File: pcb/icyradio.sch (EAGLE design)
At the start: 384 parts, among them CON301 FPC-40P, J701 TRSJACK, J702 TRSJACK, J703 TRSJACK, Q801 AO3400, Q802 AO3400, U1001 MIC23155, U1002 MIC23159, U1003 MIC2019, U1004 ADP150UJZ-1.8, U1005 ADP150UJZ-3.3, U1006 MIC94305, U1007 MIC94305, U101 EFM32GG11B420F2048GL112, U201 ATSAMS70Q21B-C, U301 ICE40HX8K-CT256, U302 SST26VF064B, U401 DSC1211DE3-C0017, U402 LTC2206, U403 RT820T2, U501 ADL5385, U502 AD9117, U503 ADL5601, U601 DSC1201DE3-50M00000, U602 ADF4351, U701 TSCS25A3X1NDGXZAX, U702 CP2615, U801 ER-TFT035-6, U901 DSC1201DE3-50M00000, U902 SI5351C, X101 32.768 kHz, X401 DNP, X901 DNP

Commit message: Production ready, ordered
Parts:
- removed R717, R718, R720, R721: 600 Ohms, Resistor:RESISTOR-0603
- removed R719, R722: 3.57 Ohms, Resistor:RESISTOR-0603
- added L701, L702, L703, L704, L705, L706: 600 Ohms, Inductor:INDUCTOR-0603
- R603: value 5.1K Ohm -> 5.1K Ohms
- U403: value RT820T2 -> R820T2; device Rafael Micro:RT820T2 -> Rafael Micro:R820T2
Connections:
- net CODEC_HP_L: now also L704.1; no longer R722.1
- net CODEC_HP_R: now also L703.1; no longer R719.1
- net CODEC_LINE_L: now also L706.1; no longer R721.1
- net CODEC_LINE_R: now also L702.1; no longer R718.1
- net CODEC_MIC_L: now also L705.1; no longer R720.1
- net CODEC_MIC_R: now also L701.1; no longer R717.1
- net N$38: now also L701.2; no longer R717.2
- net N$39: now also L705.2; no longer R720.2
- net N$42: now also L702.2; no longer R718.2
- net N$44: now also L706.2; no longer R721.2
- net N$50: now also L704.2; no longer R722.2
- net N$54: now also L703.2; no longer R719.2
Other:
- note added: "5th order Butterworth LPF fc = 10 MHz"
- note added: "FPGA_CLK1 = 49.152 MHz (for 48 kHz audio sample rate) FPGA_CLK1 = 45.1584 MHz (for 44.1 kHz audio sample rate) FPGA_CLK2 = TBD MHz (general purpose clock) FPGA_CLK3 = TBD MHz (general purpose clock) FPGA_CLK4 = TBD MHz (general purpose clock) SMC_MAIN_CLK = 50 MHz (SMC main clock) DSP_MAIN_CLK = 20 MHz (DSP main clock)"
- note added: "RXTUNER_REFCLK_SEL = 1 > 16 MHz (default) RXTUNER_REFCLK_SEL = 0 > 28.8 MHz"
- note removed: "FPGA_DDC_CLK = 49.152 MHz (for 48 kHz audio sample rate) FPGA_DDC_CLK = 45.1584 MHz (for 44.1 kHz audio sample rate) FPGA_GP_CLK1 = TBD MHz (general purpose clock) FPGA_GP_CLK2 = TBD MHz (general purpose clock) MCU_MAIN_CLK = TBD MHz (MCU main clock)"
- note removed: "TUNER_REFCLK_SEL = 1 > 16 MHz (default) TUNER_REFCLK_SEL = 0 > 28.8 MHz"
- moved on the sheet: SJ201

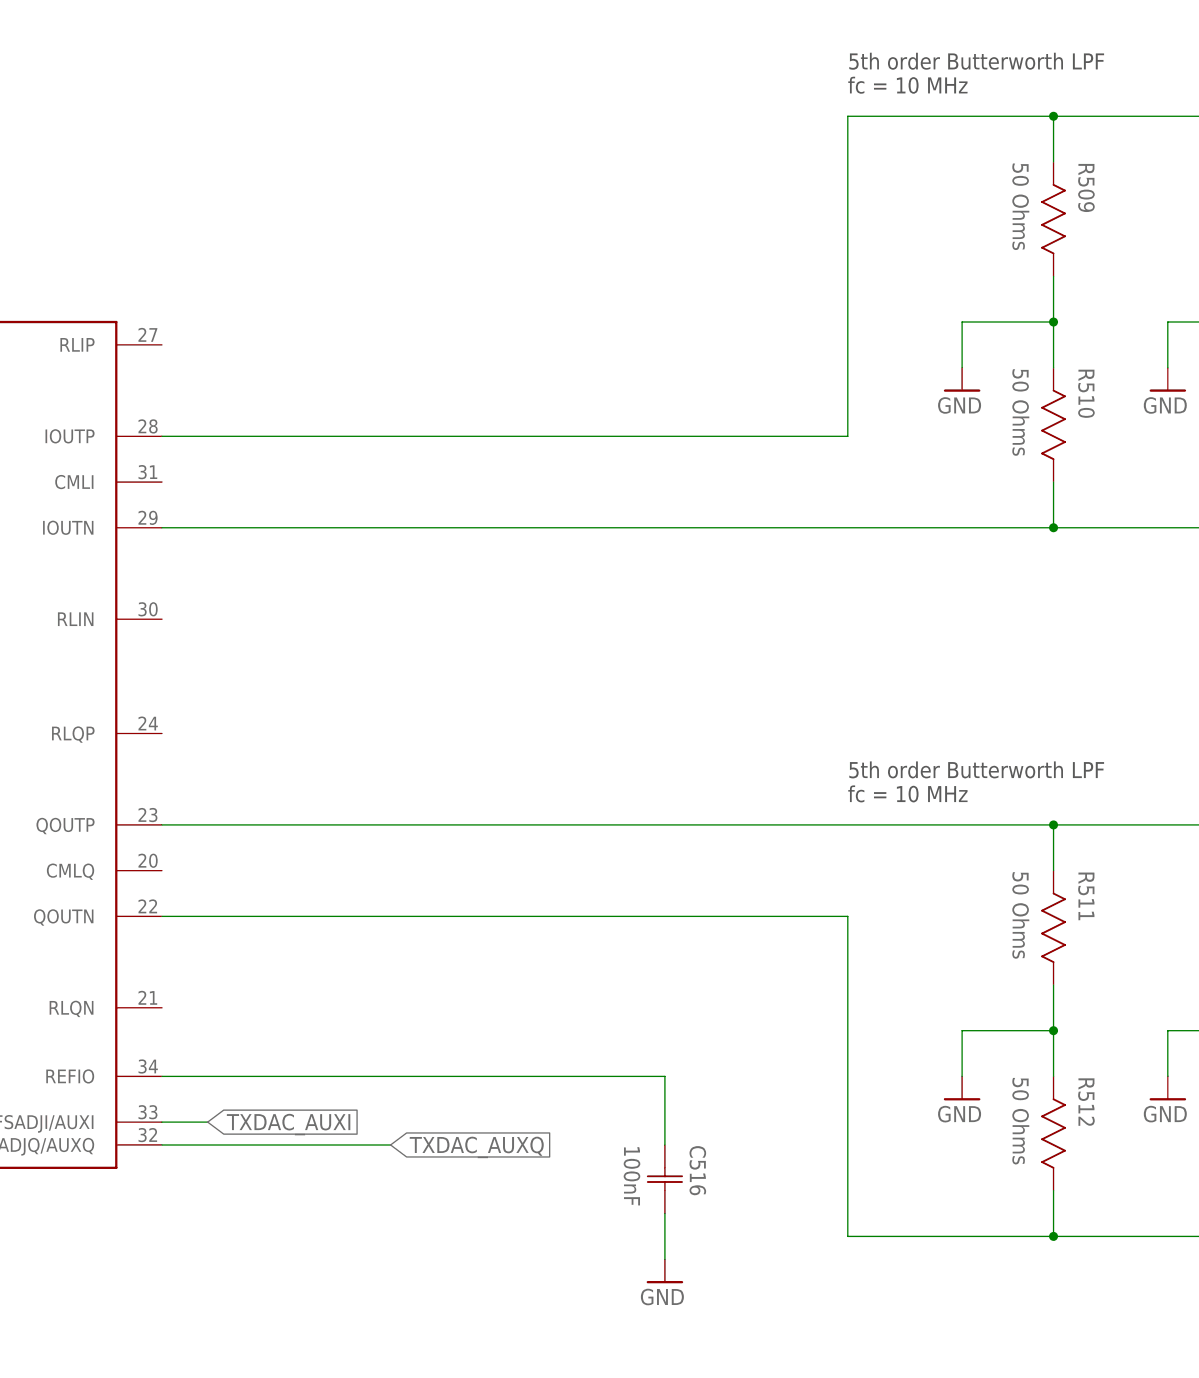
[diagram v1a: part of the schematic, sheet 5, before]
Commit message: Forgot to connect DAC common-mode, easy hardware fix tho
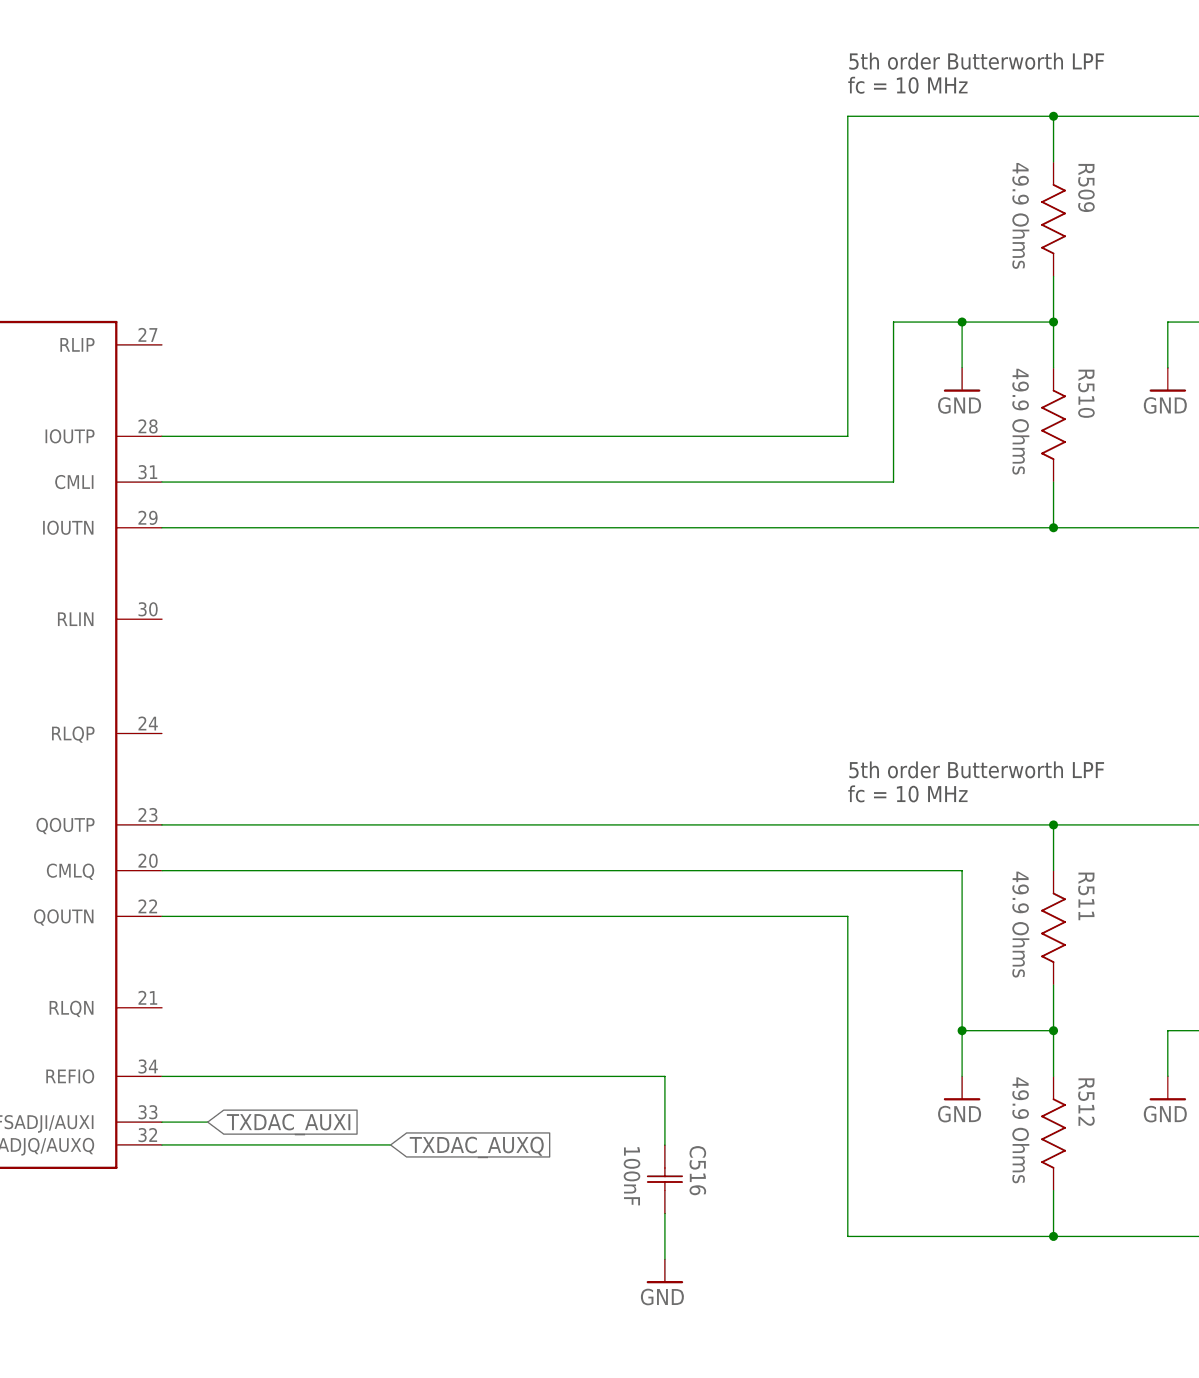
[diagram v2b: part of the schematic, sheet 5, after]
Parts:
- R509, R510, R511, R512: value 50 Ohms -> 49.9 Ohms
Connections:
- net GND: now also U502.CMLI, U502.CMLQ
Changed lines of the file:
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@@
 <part name="GND527" library="Supply Symbol" deviceset="GND" device=""/>
 <part name="L506" library="Inductor" deviceset="INDUCTOR" device="-0603" value="1.3uH"/>
-<part name="R509" library="Resistor" deviceset="RESISTOR" device="-0603" value="50 Ohms"/>
-<part name="R510" library="Resistor" deviceset="RESISTOR" device="-0603" value="50 Ohms"/>
+<part name="R509" library="Resistor" deviceset="RESISTOR" device="-0603" value="49.9 Ohms"/>
+<part name="R510" library="Resistor" deviceset="RESISTOR" device="-0603" value="49.9 Ohms"/>
 <part name="GND521" library="Supply Symbol" deviceset="GND" device=""/>
 <part name="R515" library="Resistor" deviceset="RESISTOR" device="-0603" value="100 Ohms"/>
@@
 <part name="GND528" library="Supply Symbol" deviceset="GND" device=""/>
 <part name="L508" library="Inductor" deviceset="INDUCTOR" device="-0603" value="1.3uH"/>
-<part name="R511" library="Resistor" deviceset="RESISTOR" device="-0603" value="50 Ohms"/>
-<part name="R512" library="Resistor" deviceset="RESISTOR" device="-0603" value="50 Ohms"/>
+<part name="R511" library="Resistor" deviceset="RESISTOR" device="-0603" value="49.9 Ohms"/>
+<part name="R512" library="Resistor" deviceset="RESISTOR" device="-0603" value="49.9 Ohms"/>
 <part name="GND522" library="Supply Symbol" deviceset="GND" device=""/>
 <part name="R516" library="Resistor" deviceset="RESISTOR" device="-0603" value="100 Ohms"/>
@@
 <pinref part="R509" gate="G$1" pin="1"/>
 <pinref part="R510" gate="G$1" pin="2"/>
+<pinref part="U502" gate="G$1" pin="CMLI"/>
+<wire x1="261.62" y1="276.86" x2="342.9" y2="276.86" width="0.1524" layer="91"/>
+<wire x1="342.9" y1="276.86" x2="342.9" y2="294.64" width="0.1524" layer="91"/>
+<wire x1="342.9" y1="294.64" x2="350.52" y2="294.64" width="0.1524" layer="91"/>
+<junction x="350.52" y="294.64"/>
 </segment>
 <segment>
@@
 <pinref part="R511" gate="G$1" pin="1"/>
 <pinref part="R512" gate="G$1" pin="2"/>
+<pinref part="U502" gate="G$1" pin="CMLQ"/>
+<wire x1="261.62" y1="233.68" x2="350.52" y2="233.68" width="0.1524" layer="91"/>
+<wire x1="350.52" y1="233.68" x2="350.52" y2="215.9" width="0.1524" layer="91"/>
+<junction x="350.52" y="215.9"/>
 </segment>
 <segment>
